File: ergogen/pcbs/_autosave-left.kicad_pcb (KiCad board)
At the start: 2 copper layers, 167 x 141 mm, 62 parts

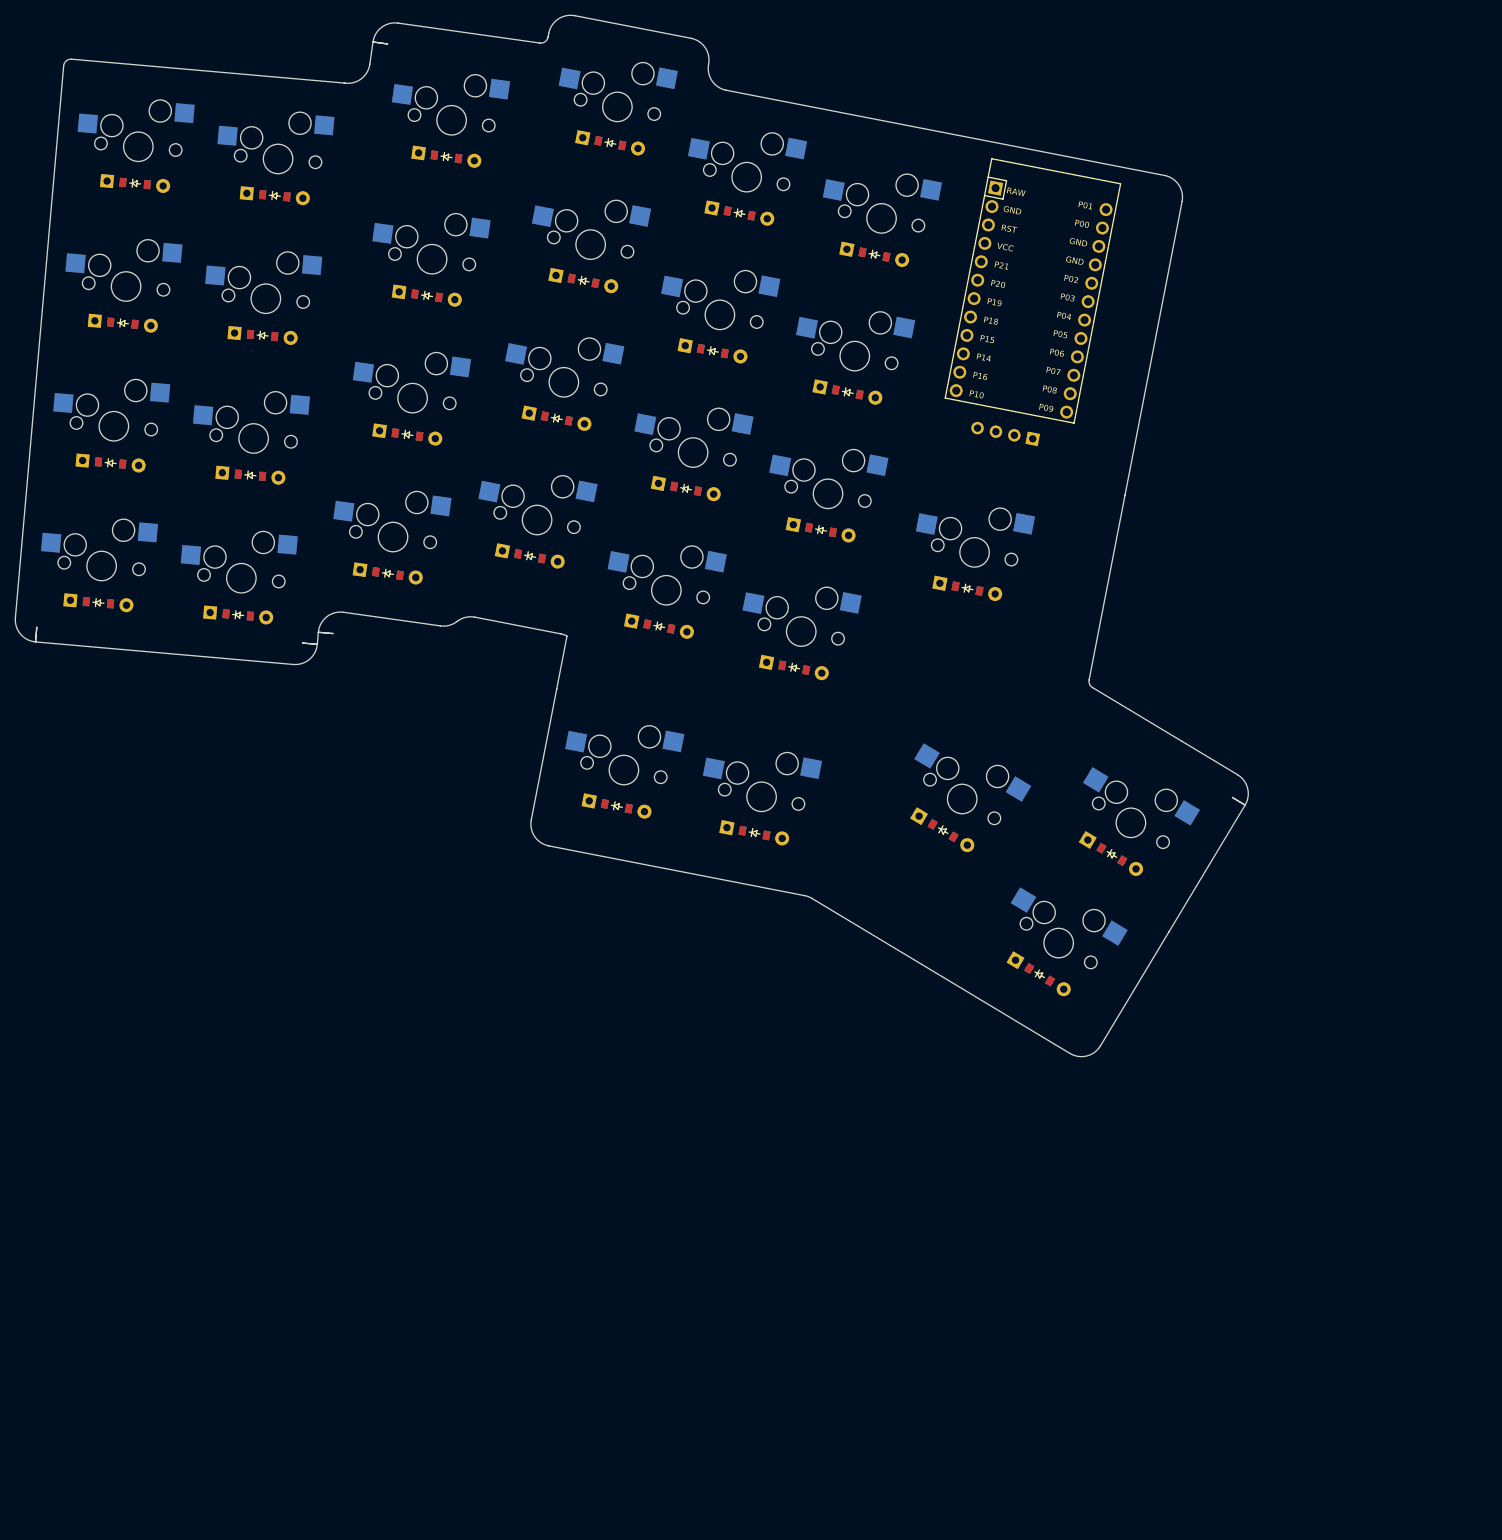
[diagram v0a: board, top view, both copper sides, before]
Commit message: decided to go reversible pcb route, removed right side and added reversible components to left side
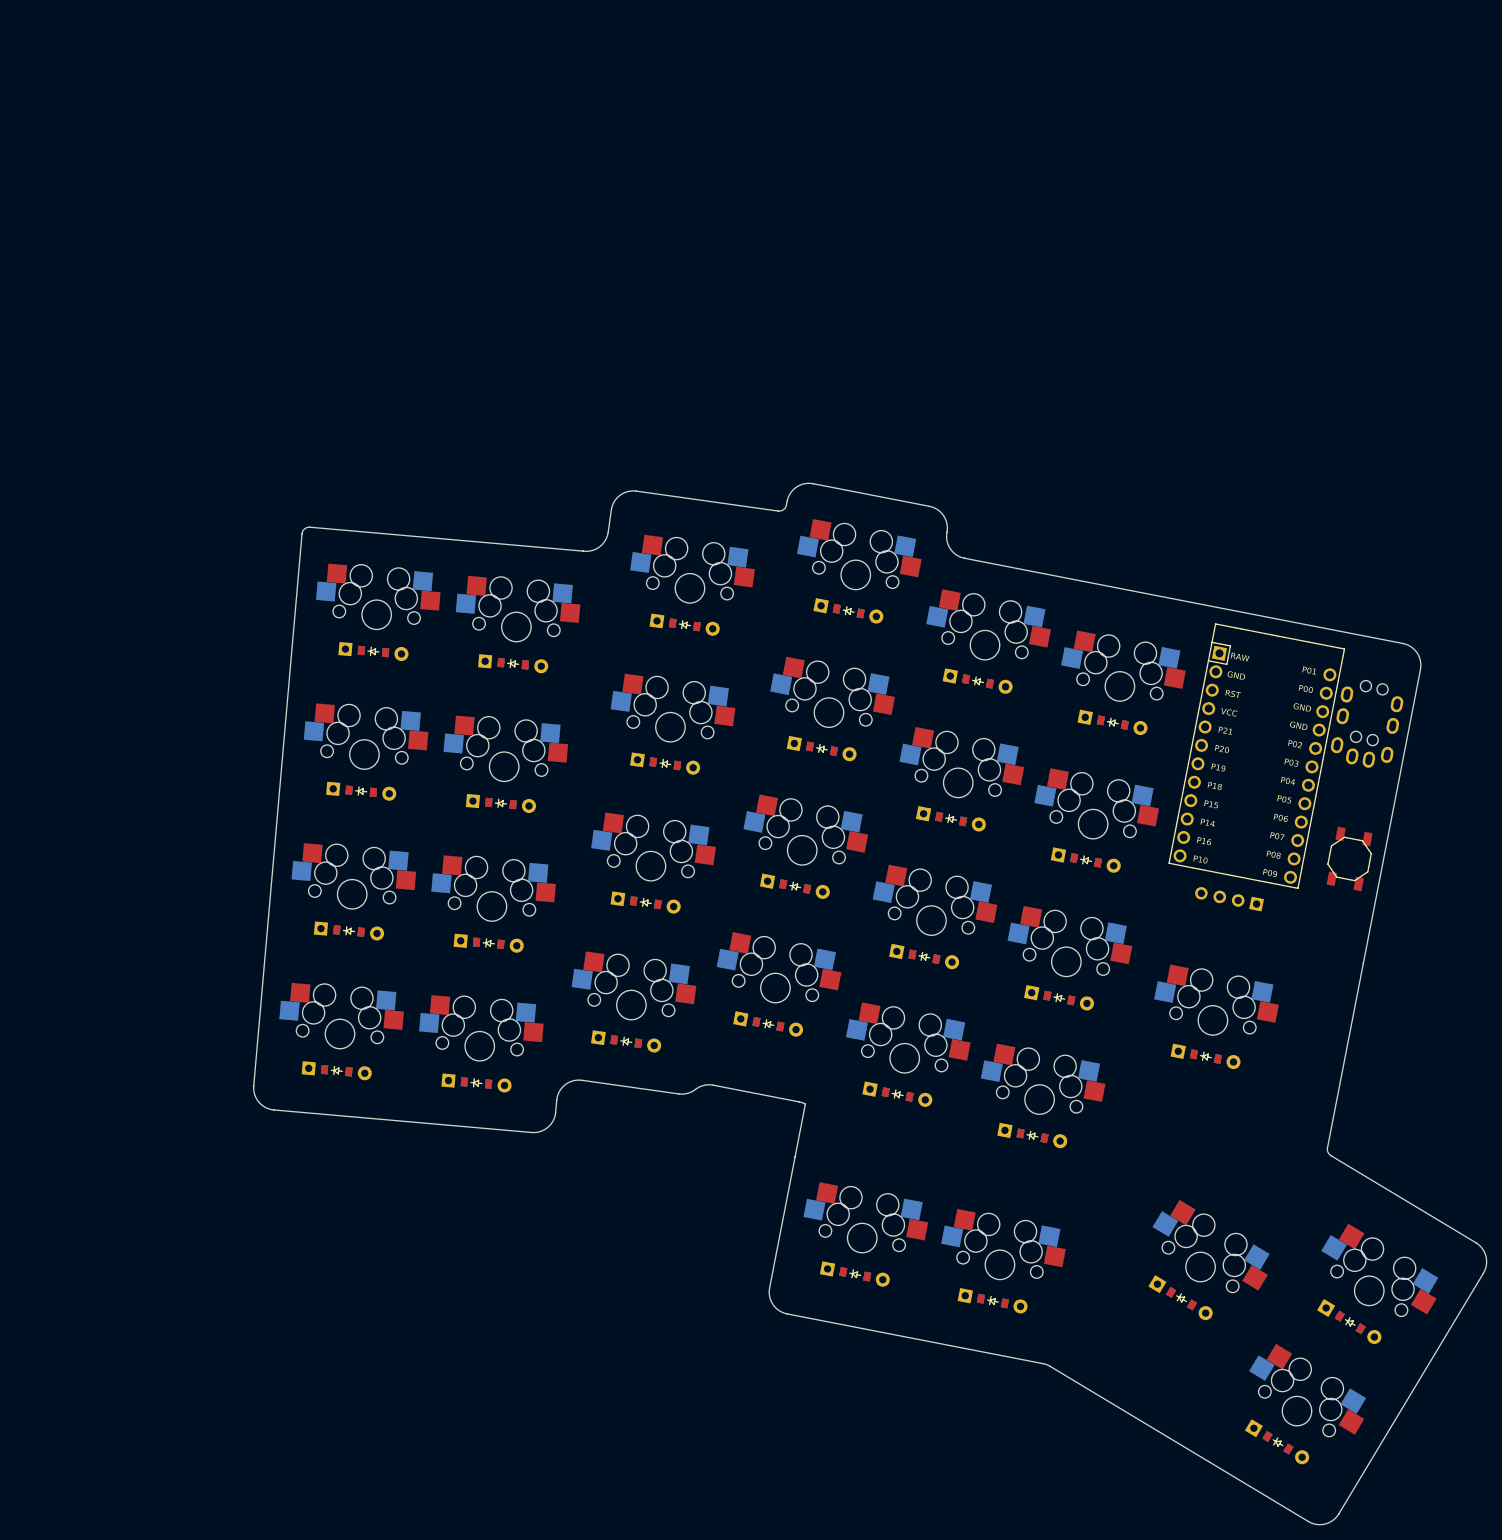
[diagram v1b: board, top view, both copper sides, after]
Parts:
- added B1: , E73:SW_TACT_ALPS_SKQGABE010, F.Cu at (209.2, 141.4)
- added TRRS1: TRRS-PJ-320A-dual, TRRS-PJ-320A-dual, F.Cu at (213.9, 116.8)
- moved D22 71.1 mm to (169.9, 160.2)
- moved S25 71.1 mm to (190.7, 163.2)
- moved S29 71.1 mm to (202.1, 216.2)
- moved D10 71.1 mm to (113.9, 147.3)
- moved D13 71.1 mm to (130.5, 163.8)
- moved D15 71.1 mm to (137.7, 126.5)
- moved D16 71.1 mm to (141.3, 107.8)
- moved D18 71.1 mm to (151.6, 154.6)
- moved D2 71.1 mm to (73.7, 151.1)
- moved D24 71.1 mm to (177.1, 122.9)
- moved D25 71.1 mm to (189.7, 168.2)
- moved D26 71.1 mm to (142.2, 197.6)
- moved D27 71.1 mm to (160.9, 201.3)
- moved D7 71.1 mm to (94.2, 133.9)
- moved D8 71.1 mm to (95.9, 114.9)
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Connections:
- D1 pad 1: (no net) -> P7
- D10 pad 1: (no net) -> P6
- D11 pad 1: (no net) -> P5
- D12 pad 1: (no net) -> P4
- D13 pad 1: (no net) -> P7
- D14 pad 1: (no net) -> P6
- D15 pad 1: (no net) -> P5
- D16 pad 1: (no net) -> P4
- D17 pad 1: (no net) -> P7
- D18 pad 1: (no net) -> P6
- D19 pad 1: (no net) -> P5
- D2 pad 1: (no net) -> P6
- D20 pad 1: (no net) -> P4
- D21 pad 1: (no net) -> P7
- D22 pad 1: (no net) -> P6
- D23 pad 1: (no net) -> P5
- D24 pad 1: (no net) -> P4
- D25 pad 1: (no net) -> P7
- D26 pad 1: (no net) -> P9
- D27 pad 1: (no net) -> P9
- D28 pad 1: (no net) -> P9
- D29 pad 1: (no net) -> P9
- D3 pad 1: (no net) -> P5
- D30 pad 1: (no net) -> P8
- D4 pad 1: (no net) -> P4
- D5 pad 1: (no net) -> P7
- D6 pad 1: (no net) -> P6
- D7 pad 1: (no net) -> P5
- D8 pad 1: (no net) -> P4
- D9 pad 1: (no net) -> P7
- S1 pad 1: (no net) -> P21
- S10 pad 1: (no net) -> P19
- S11 pad 1: (no net) -> P19
- S12 pad 1: (no net) -> P19
- S13 pad 1: (no net) -> P18
- S14 pad 1: (no net) -> P18
- S15 pad 1: (no net) -> P18
- S16 pad 1: (no net) -> P18
- S17 pad 1: (no net) -> P15
- S18 pad 1: (no net) -> P15
- S19 pad 1: (no net) -> P15
- S2 pad 1: (no net) -> P21
- S20 pad 1: (no net) -> P15
- S21 pad 1: (no net) -> P14
- S22 pad 1: (no net) -> P14
- S23 pad 1: (no net) -> P14
- S24 pad 1: (no net) -> P14
- S25 pad 1: (no net) -> P16
- S26 pad 1: (no net) -> P18
- S27 pad 1: (no net) -> P15
- S28 pad 1: (no net) -> P14
- S29 pad 1: (no net) -> P16
- S3 pad 1: (no net) -> P21
- S30 pad 1: (no net) -> P16
- S4 pad 1: (no net) -> P21
- S5 pad 1: (no net) -> P20
- S6 pad 1: (no net) -> P20
- S7 pad 1: (no net) -> P20
- S8 pad 1: (no net) -> P20
- S9 pad 1: (no net) -> P19
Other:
- outline, holes or cut-outs redrawn
